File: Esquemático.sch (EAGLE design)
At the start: 4 parts, among them U1 MPU-6050-1, U2 MPU-6050-1, U3 MPU-6050-1

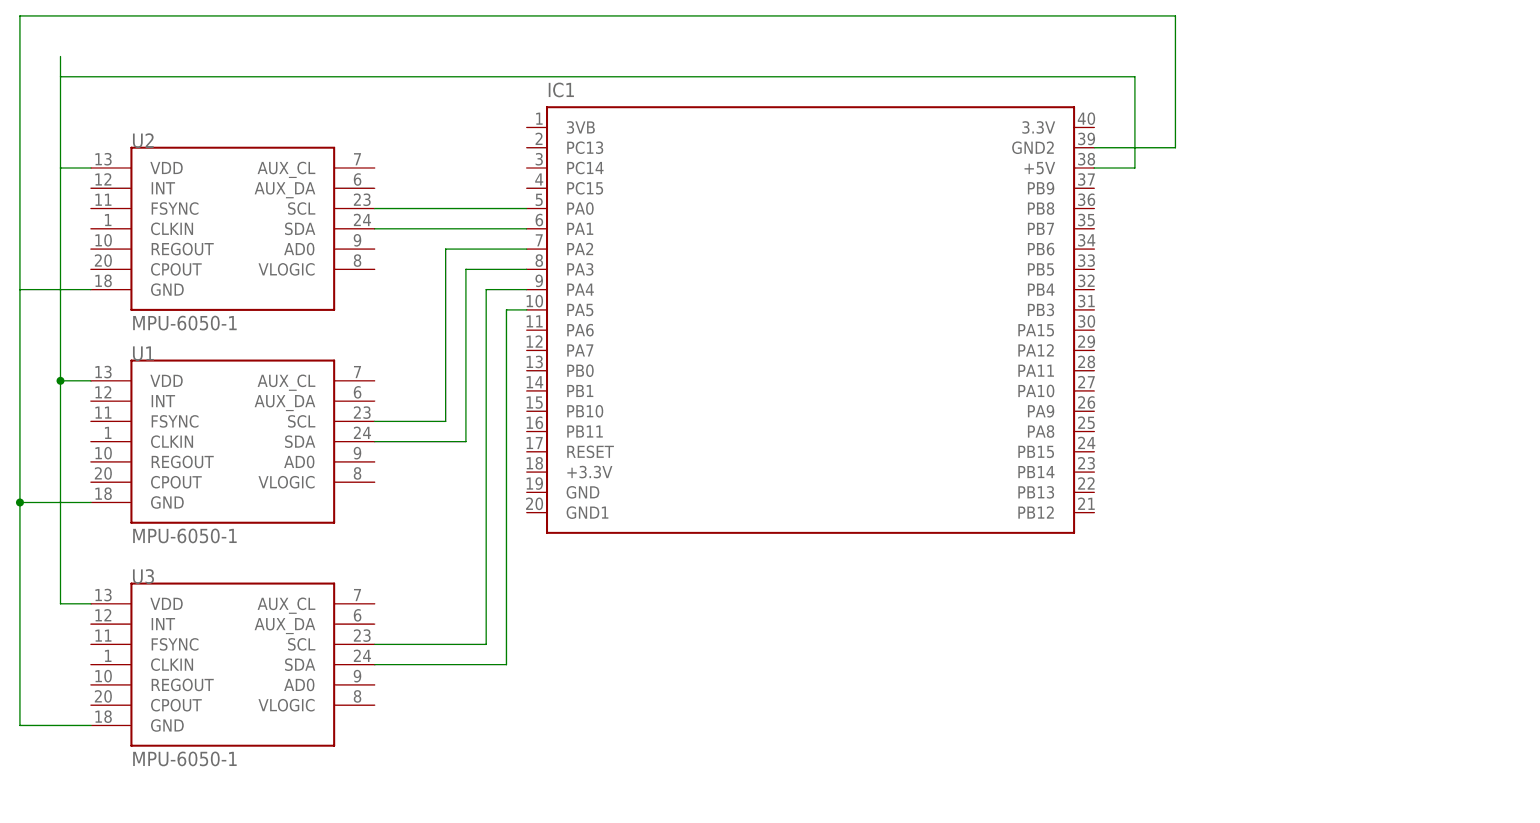
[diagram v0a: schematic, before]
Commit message: Esquemático
Agora usando comunicação I2C
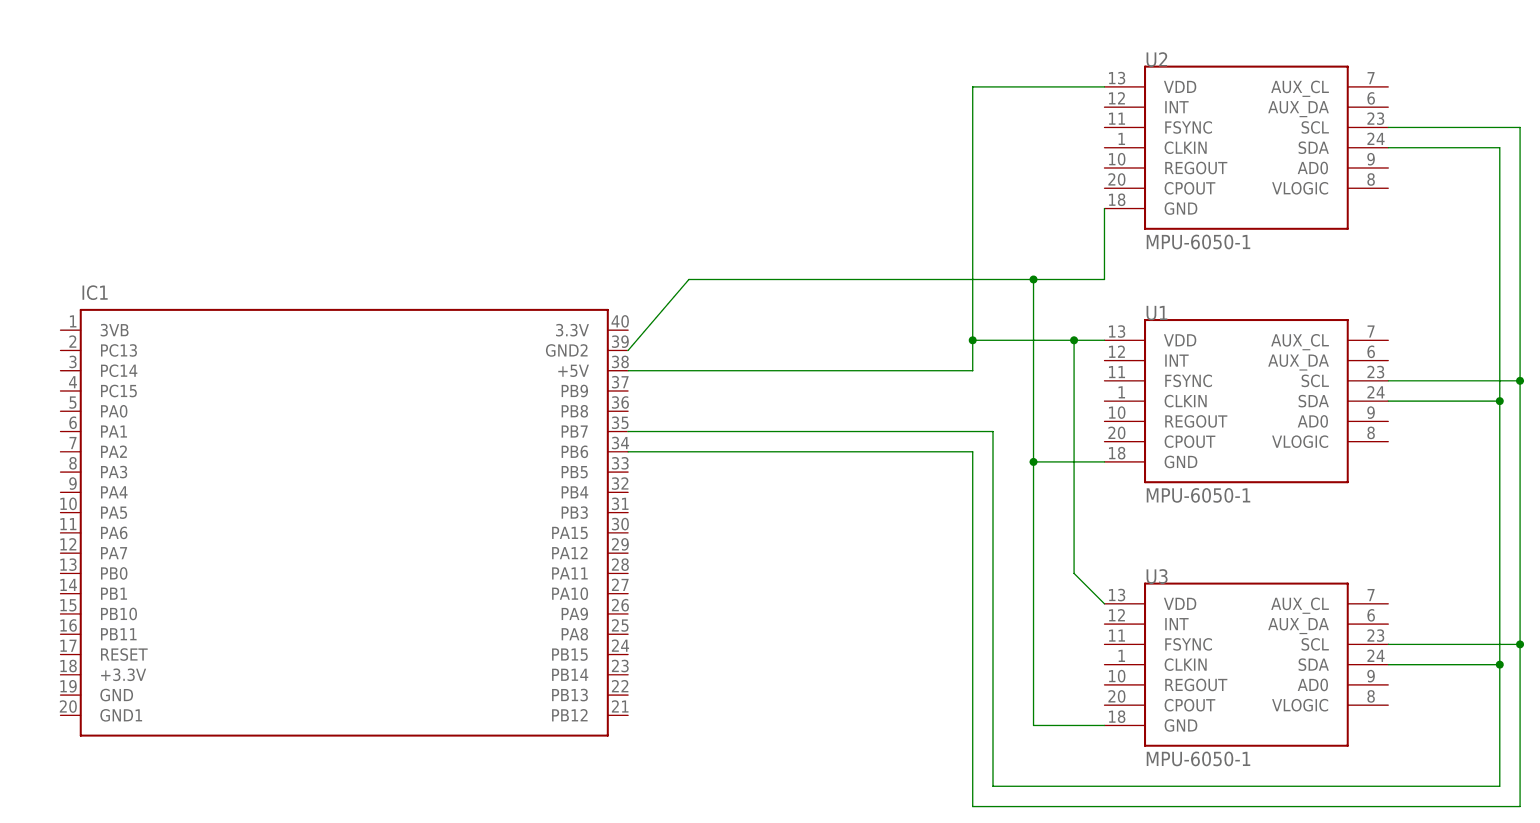
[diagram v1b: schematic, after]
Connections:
- removed net N$3 (its old number): IC1.PA2, U1.SCL
- removed net N$4 (its old number): IC1.PA3, U1.SDA
- removed net N$5: IC1.PA4, U3.SCL
- removed net N$6: IC1.PA5, U3.SDA
- net N$1: now also IC1.PB6, U1.SCL, U3.SCL; no longer IC1.PA0
- net N$2: now also IC1.PB7, U1.SDA, U3.SDA; no longer IC1.PA1
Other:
- moved on the sheet: IC1, U1, U2, U3
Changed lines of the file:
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@@
 <setting verticaltext="up"/>
 </settings>
-<grid distance="0.1" unitdist="inch" unit="inch" style="lines" multiple="1" display="yes" altdistance="0.01" altunitdist="inch" altunit="inch"/>
+<grid distance="0.1" unitdist="inch" unit="mm" style="lines" multiple="1" display="yes" altdistance="0.01" altunitdist="inch" altunit="inch"/>
 <layers>
 <layer number="1" name="Top" color="4" fill="1" visible="no" active="no"/>
@@
 </plain>
 <instances>
-<instance part="IC1" gate="G$1" x="30.48" y="52.07"/>
-<instance part="U1" gate="G$1" x="-41.91" y="38.1"/>
-<instance part="U2" gate="G$1" x="-41.91" y="64.77"/>
-<instance part="U3" gate="G$1" x="-41.91" y="10.16"/>
+<instance part="IC1" gate="G$1" x="-27.94" y="26.67"/>
+<instance part="U1" gate="G$1" x="85.09" y="43.18"/>
+<instance part="U2" gate="G$1" x="85.09" y="74.93"/>
+<instance part="U3" gate="G$1" x="85.09" y="10.16"/>
 </instances>
 <busses>
@@
 <net name="N$1" class="0">
 <segment>
+<pinref part="IC1" gate="G$1" pin="PB6"/>
+<wire x1="7.62" y1="36.83" x2="50.8" y2="36.83" width="0.1524" layer="91"/>
+<wire x1="50.8" y1="36.83" x2="50.8" y2="-7.62" width="0.1524" layer="91"/>
+<wire x1="50.8" y1="-7.62" x2="119.38" y2="-7.62" width="0.1524" layer="91"/>
+<wire x1="119.38" y1="-7.62" x2="119.38" y2="12.7" width="0.1524" layer="91"/>
 <pinref part="U2" gate="G$1" pin="SCL"/>
-<pinref part="IC1" gate="G$1" pin="PA0"/>
-<wire x1="-24.13" y1="67.31" x2="-5.08" y2="67.31" width="0.1524" layer="91"/>
+<wire x1="119.38" y1="12.7" x2="119.38" y2="45.72" width="0.1524" layer="91"/>
+<wire x1="119.38" y1="45.72" x2="119.38" y2="77.47" width="0.1524" layer="91"/>
+<wire x1="119.38" y1="77.47" x2="102.87" y2="77.47" width="0.1524" layer="91"/>
+<pinref part="U1" gate="G$1" pin="SCL"/>
+<wire x1="102.87" y1="45.72" x2="119.38" y2="45.72" width="0.1524" layer="91"/>
+<junction x="119.38" y="45.72"/>
+<pinref part="U3" gate="G$1" pin="SCL"/>
+<wire x1="102.87" y1="12.7" x2="119.38" y2="12.7" width="0.1524" layer="91"/>
+<junction x="119.38" y="12.7"/>
 </segment>
 </net>
 <net name="N$2" class="0">
 <segment>
+<pinref part="IC1" gate="G$1" pin="PB7"/>
+<wire x1="7.62" y1="39.37" x2="53.34" y2="39.37" width="0.1524" layer="91"/>
+<wire x1="53.34" y1="39.37" x2="53.34" y2="-5.08" width="0.1524" layer="91"/>
+<wire x1="53.34" y1="-5.08" x2="116.84" y2="-5.08" width="0.1524" layer="91"/>
 <pinref part="U2" gate="G$1" pin="SDA"/>
-<pinref part="IC1" gate="G$1" pin="PA1"/>
-<wire x1="-24.13" y1="64.77" x2="-5.08" y2="64.77" width="0.1524" layer="91"/>
+<wire x1="116.84" y1="-5.08" x2="116.84" y2="10.16" width="0.1524" layer="91"/>
+<wire x1="116.84" y1="10.16" x2="116.84" y2="43.18" width="0.1524" layer="91"/>
+<wire x1="116.84" y1="43.18" x2="116.84" y2="74.93" width="0.1524" layer="91"/>
+<wire x1="116.84" y1="74.93" x2="102.87" y2="74.93" width="0.1524" layer="91"/>
+<pinref part="U1" gate="G$1" pin="SDA"/>
+<wire x1="102.87" y1="43.18" x2="116.84" y2="43.18" width="0.1524" layer="91"/>
+<junction x="116.84" y="43.18"/>
+<pinref part="U3" gate="G$1" pin="SDA"/>
+<wire x1="102.87" y1="10.16" x2="116.84" y2="10.16" width="0.1524" layer="91"/>
+<junction x="116.84" y="10.16"/>
 </segment>
 </net>
 <net name="N$3" class="0">
 <segment>
-<pinref part="IC1" gate="G$1" pin="PA2"/>
-<wire x1="-5.08" y1="62.23" x2="-15.24" y2="62.23" width="0.1524" layer="91"/>
-<wire x1="-15.24" y1="62.23" x2="-15.24" y2="40.64" width="0.1524" layer="91"/>
-<pinref part="U1" gate="G$1" pin="SCL"/>
-<wire x1="-15.24" y1="40.64" x2="-24.13" y2="40.64" width="0.1524" layer="91"/>
+<pinref part="U2" gate="G$1" pin="VDD"/>
+<wire x1="67.31" y1="82.55" x2="50.8" y2="82.55" width="0.1524" layer="91"/>
+<wire x1="50.8" y1="82.55" x2="50.8" y2="50.8" width="0.1524" layer="91"/>
+<pinref part="IC1" gate="G$1" pin="+5V"/>
+<wire x1="50.8" y1="50.8" x2="50.8" y2="46.99" width="0.1524" layer="91"/>
+<wire x1="7.62" y1="46.99" x2="50.8" y2="46.99" width="0.1524" layer="91"/>
+<pinref part="U1" gate="G$1" pin="VDD"/>
+<wire x1="67.31" y1="50.8" x2="63.5" y2="50.8" width="0.1524" layer="91"/>
+<junction x="50.8" y="50.8"/>
+<pinref part="U3" gate="G$1" pin="VDD"/>
+<wire x1="63.5" y1="50.8" x2="50.8" y2="50.8" width="0.1524" layer="91"/>
+<wire x1="67.31" y1="17.78" x2="63.5" y2="21.59" width="0.1524" layer="91"/>
+<wire x1="63.5" y1="21.59" x2="63.5" y2="50.8" width="0.1524" layer="91"/>
+<junction x="63.5" y="50.8"/>
 </segment>
 </net>
 <net name="N$4" class="0">
 <segment>
-<pinref part="U1" gate="G$1" pin="SDA"/>
-<wire x1="-24.13" y1="38.1" x2="-12.7" y2="38.1" width="0.1524" layer="91"/>
-<wire x1="-12.7" y1="38.1" x2="-12.7" y2="59.69" width="0.1524" layer="91"/>
-<pinref part="IC1" gate="G$1" pin="PA3"/>
-<wire x1="-5.08" y1="59.69" x2="-12.7" y2="59.69" width="0.1524" layer="91"/>
-</segment>
-</net>
-<net name="N$5" class="0">
-<segment>
-<pinref part="IC1" gate="G$1" pin="PA4"/>
-<wire x1="-5.08" y1="57.15" x2="-10.16" y2="57.15" width="0.1524" layer="91"/>
-<pinref part="U3" gate="G$1" pin="SCL"/>
-<wire x1="-10.16" y1="57.15" x2="-10.16" y2="12.7" width="0.1524" layer="91"/>
-<wire x1="-10.16" y1="12.7" x2="-24.13" y2="12.7" width="0.1524" layer="91"/>
-</segment>
-</net>
-<net name="N$6" class="0">
-<segment>
-<pinref part="IC1" gate="G$1" pin="PA5"/>
-<wire x1="-5.08" y1="54.61" x2="-7.62" y2="54.61" width="0.1524" layer="91"/>
-<wire x1="-7.62" y1="54.61" x2="-7.62" y2="10.16" width="0.1524" layer="91"/>
-<pinref part="U3" gate="G$1" pin="SDA"/>
-<wire x1="-7.62" y1="10.16" x2="-24.13" y2="10.16" width="0.1524" layer="91"/>
-</segment>
-</net>
-<net name="N$7" class="0">
-<segment>
-<pinref part="U2" gate="G$1" pin="VDD"/>
-<wire x1="-59.69" y1="72.39" x2="-63.5" y2="72.39" width="0.1524" layer="91"/>
-<wire x1="-63.5" y1="72.39" x2="-63.5" y2="83.82" width="0.1524" layer="91"/>
-<wire x1="-63.5" y1="86.36" x2="-63.5" y2="83.82" width="0.1524" layer="91"/>
-<wire x1="-63.5" y1="83.82" x2="71.12" y2="83.82" width="0.1524" layer="91"/>
-<pinref part="IC1" gate="G$1" pin="+5V"/>
-<wire x1="71.12" y1="83.82" x2="71.12" y2="72.39" width="0.1524" layer="91"/>
-<wire x1="71.12" y1="72.39" x2="66.04" y2="72.39" width="0.1524" layer="91"/>
-<pinref part="U1" gate="G$1" pin="VDD"/>
-<wire x1="-59.69" y1="45.72" x2="-63.5" y2="45.72" width="0.1524" layer="91"/>
-<wire x1="-63.5" y1="45.72" x2="-63.5" y2="72.39" width="0.1524" layer="91"/>
-<pinref part="U3" gate="G$1" pin="VDD"/>
-<wire x1="-59.69" y1="17.78" x2="-63.5" y2="17.78" width="0.1524" layer="91"/>
-<wire x1="-63.5" y1="17.78" x2="-63.5" y2="45.72" width="0.1524" layer="91"/>
-<junction x="-63.5" y="45.72"/>
-</segment>
-</net>
-<net name="N$8" class="0">
-<segment>
+<pinref part="U1" gate="G$1" pin="GND"/>
+<wire x1="67.31" y1="35.56" x2="58.42" y2="35.56" width="0.1524" layer="91"/>
+<wire x1="58.42" y1="35.56" x2="58.42" y2="58.42" width="0.1524" layer="91"/>
+<wire x1="58.42" y1="58.42" x2="15.24" y2="58.42" width="0.1524" layer="91"/>
 <pinref part="IC1" gate="G$1" pin="GND2"/>
-<wire x1="66.04" y1="74.93" x2="76.2" y2="74.93" width="0.1524" layer="91"/>
-<wire x1="76.2" y1="74.93" x2="76.2" y2="91.44" width="0.1524" layer="91"/>
-<wire x1="76.2" y1="91.44" x2="-68.58" y2="91.44" width="0.1524" layer="91"/>
+<wire x1="15.24" y1="58.42" x2="7.62" y2="49.53" width="0.1524" layer="91"/>
 <pinref part="U2" gate="G$1" pin="GND"/>
-<wire x1="-68.58" y1="91.44" x2="-68.58" y2="57.15" width="0.1524" layer="91"/>
-<wire x1="-68.58" y1="57.15" x2="-59.69" y2="57.15" width="0.1524" layer="91"/>
-<pinref part="U1" gate="G$1" pin="GND"/>
-<wire x1="-59.69" y1="30.48" x2="-68.58" y2="30.48" width="0.1524" layer="91"/>
-<wire x1="-68.58" y1="30.48" x2="-68.58" y2="57.15" width="0.1524" layer="91"/>
+<wire x1="58.42" y1="58.42" x2="67.31" y2="58.42" width="0.1524" layer="91"/>
+<wire x1="67.31" y1="58.42" x2="67.31" y2="67.31" width="0.1524" layer="91"/>
+<junction x="58.42" y="58.42"/>
+<wire x1="58.42" y1="35.56" x2="58.42" y2="2.54" width="0.1524" layer="91"/>
+<junction x="58.42" y="35.56"/>
 <pinref part="U3" gate="G$1" pin="GND"/>
-<wire x1="-59.69" y1="2.54" x2="-68.58" y2="2.54" width="0.1524" layer="91"/>
-<wire x1="-68.58" y1="2.54" x2="-68.58" y2="30.48" width="0.1524" layer="91"/>
-<junction x="-68.58" y="30.48"/>
-</segment>
-</net>
+<wire x1="58.42" y1="2.54" x2="67.31" y2="2.54" width="0.1524" layer="91"/>
+</segment>
+</net>

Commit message: Última versão do Esquemático
Presentes tanto:
Esquemático.pdf
Esquemático.png
Esquemático.sch
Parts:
- removed U3: MPU-6050-1, Testing:MPU-6050-1
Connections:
- new net N$5: IC1.+5V, U1.VDD, U2.VDD
- new net N$6: IC1.GND2, U1.GND
- new net N$7: IC1.GND, U2.GND
- net N$1: now also IC1.PB10; no longer IC1.PB6, U1.SCL, U3.SCL
- net N$2: no longer U2.SDA, U3.SDA
- net N$3: now also IC1.PB6, U1.SCL; no longer IC1.+5V, U1.VDD, U2.VDD, U3.VDD
- net N$4: now also IC1.PB11, U2.SDA; no longer IC1.GND2, U1.GND, U2.GND, U3.GND
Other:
- moved on the sheet: IC1, U1, U2
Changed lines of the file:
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@@
 <part name="U1" library="Testing" deviceset="MPU-6050" device="-1"/>
 <part name="U2" library="Testing" deviceset="MPU-6050" device="-1"/>
-<part name="U3" library="Testing" deviceset="MPU-6050" device="-1"/>
 </parts>
 <sheets>
@@
 </plain>
 <instances>
-<instance part="IC1" gate="G$1" x="-27.94" y="26.67"/>
-<instance part="U1" gate="G$1" x="85.09" y="43.18"/>
-<instance part="U2" gate="G$1" x="85.09" y="74.93"/>
-<instance part="U3" gate="G$1" x="85.09" y="10.16"/>
+<instance part="IC1" gate="G$1" x="27.94" y="26.67"/>
+<instance part="U1" gate="G$1" x="90.17" y="71.12"/>
+<instance part="U2" gate="G$1" x="-46.99" y="13.97"/>
 </instances>
 <busses>
@@
 <net name="N$1" class="0">
 <segment>
+<pinref part="U2" gate="G$1" pin="SCL"/>
+<pinref part="IC1" gate="G$1" pin="PB10"/>
+<wire x1="-29.21" y1="16.51" x2="-7.62" y2="16.51" width="0.1524" layer="91"/>
+</segment>
+</net>
+<net name="N$3" class="0">
+<segment>
+<pinref part="U1" gate="G$1" pin="SCL"/>
+<wire x1="107.95" y1="73.66" x2="116.84" y2="73.66" width="0.1524" layer="91"/>
 <pinref part="IC1" gate="G$1" pin="PB6"/>
-<wire x1="7.62" y1="36.83" x2="50.8" y2="36.83" width="0.1524" layer="91"/>
-<wire x1="50.8" y1="36.83" x2="50.8" y2="-7.62" width="0.1524" layer="91"/>
-<wire x1="50.8" y1="-7.62" x2="119.38" y2="-7.62" width="0.1524" layer="91"/>
-<wire x1="119.38" y1="-7.62" x2="119.38" y2="12.7" width="0.1524" layer="91"/>
-<pinref part="U2" gate="G$1" pin="SCL"/>
-<wire x1="119.38" y1="12.7" x2="119.38" y2="45.72" width="0.1524" layer="91"/>
-<wire x1="119.38" y1="45.72" x2="119.38" y2="77.47" width="0.1524" layer="91"/>
-<wire x1="119.38" y1="77.47" x2="102.87" y2="77.47" width="0.1524" layer="91"/>
-<pinref part="U1" gate="G$1" pin="SCL"/>
-<wire x1="102.87" y1="45.72" x2="119.38" y2="45.72" width="0.1524" layer="91"/>
-<junction x="119.38" y="45.72"/>
-<pinref part="U3" gate="G$1" pin="SCL"/>
-<wire x1="102.87" y1="12.7" x2="119.38" y2="12.7" width="0.1524" layer="91"/>
-<junction x="119.38" y="12.7"/>
+<wire x1="63.5" y1="36.83" x2="116.84" y2="36.83" width="0.1524" layer="91"/>
+<wire x1="116.84" y1="36.83" x2="116.84" y2="73.66" width="0.1524" layer="91"/>
 </segment>
 </net>
@@
 <segment>
 <pinref part="IC1" gate="G$1" pin="PB7"/>
-<wire x1="7.62" y1="39.37" x2="53.34" y2="39.37" width="0.1524" layer="91"/>
-<wire x1="53.34" y1="39.37" x2="53.34" y2="-5.08" width="0.1524" layer="91"/>
-<wire x1="53.34" y1="-5.08" x2="116.84" y2="-5.08" width="0.1524" layer="91"/>
-<pinref part="U2" gate="G$1" pin="SDA"/>
-<wire x1="116.84" y1="-5.08" x2="116.84" y2="10.16" width="0.1524" layer="91"/>
-<wire x1="116.84" y1="10.16" x2="116.84" y2="43.18" width="0.1524" layer="91"/>
-<wire x1="116.84" y1="43.18" x2="116.84" y2="74.93" width="0.1524" layer="91"/>
-<wire x1="116.84" y1="74.93" x2="102.87" y2="74.93" width="0.1524" layer="91"/>
+<wire x1="63.5" y1="39.37" x2="114.3" y2="39.37" width="0.1524" layer="91"/>
+<wire x1="114.3" y1="39.37" x2="114.3" y2="71.12" width="0.1524" layer="91"/>
 <pinref part="U1" gate="G$1" pin="SDA"/>
-<wire x1="102.87" y1="43.18" x2="116.84" y2="43.18" width="0.1524" layer="91"/>
-<junction x="116.84" y="43.18"/>
-<pinref part="U3" gate="G$1" pin="SDA"/>
-<wire x1="102.87" y1="10.16" x2="116.84" y2="10.16" width="0.1524" layer="91"/>
-<junction x="116.84" y="10.16"/>
-</segment>
-</net>
-<net name="N$3" class="0">
-<segment>
-<pinref part="U2" gate="G$1" pin="VDD"/>
-<wire x1="67.31" y1="82.55" x2="50.8" y2="82.55" width="0.1524" layer="91"/>
-<wire x1="50.8" y1="82.55" x2="50.8" y2="50.8" width="0.1524" layer="91"/>
-<pinref part="IC1" gate="G$1" pin="+5V"/>
-<wire x1="50.8" y1="50.8" x2="50.8" y2="46.99" width="0.1524" layer="91"/>
-<wire x1="7.62" y1="46.99" x2="50.8" y2="46.99" width="0.1524" layer="91"/>
-<pinref part="U1" gate="G$1" pin="VDD"/>
-<wire x1="67.31" y1="50.8" x2="63.5" y2="50.8" width="0.1524" layer="91"/>
-<junction x="50.8" y="50.8"/>
-<pinref part="U3" gate="G$1" pin="VDD"/>
-<wire x1="63.5" y1="50.8" x2="50.8" y2="50.8" width="0.1524" layer="91"/>
-<wire x1="67.31" y1="17.78" x2="63.5" y2="21.59" width="0.1524" layer="91"/>
-<wire x1="63.5" y1="21.59" x2="63.5" y2="50.8" width="0.1524" layer="91"/>
-<junction x="63.5" y="50.8"/>
+<wire x1="114.3" y1="71.12" x2="107.95" y2="71.12" width="0.1524" layer="91"/>
 </segment>
 </net>
 <net name="N$4" class="0">
 <segment>
-<pinref part="U1" gate="G$1" pin="GND"/>
-<wire x1="67.31" y1="35.56" x2="58.42" y2="35.56" width="0.1524" layer="91"/>
-<wire x1="58.42" y1="35.56" x2="58.42" y2="58.42" width="0.1524" layer="91"/>
-<wire x1="58.42" y1="58.42" x2="15.24" y2="58.42" width="0.1524" layer="91"/>
-<pinref part="IC1" gate="G$1" pin="GND2"/>
-<wire x1="15.24" y1="58.42" x2="7.62" y2="49.53" width="0.1524" layer="91"/>
-<pinref part="U2" gate="G$1" pin="GND"/>
-<wire x1="58.42" y1="58.42" x2="67.31" y2="58.42" width="0.1524" layer="91"/>
-<wire x1="67.31" y1="58.42" x2="67.31" y2="67.31" width="0.1524" layer="91"/>
-<junction x="58.42" y="58.42"/>
-<wire x1="58.42" y1="35.56" x2="58.42" y2="2.54" width="0.1524" layer="91"/>
-<junction x="58.42" y="35.56"/>
-<pinref part="U3" gate="G$1" pin="GND"/>
-<wire x1="58.42" y1="2.54" x2="67.31" y2="2.54" width="0.1524" layer="91"/>
+<pinref part="U2" gate="G$1" pin="SDA"/>
+<pinref part="IC1" gate="G$1" pin="PB11"/>
+<wire x1="-29.21" y1="13.97" x2="-7.62" y2="13.97" width="0.1524" layer="91"/>
 </segment>
 </net>
+<net name="N$5" class="0">
+<segment>
+<pinref part="U1" gate="G$1" pin="VDD"/>
+<wire x1="72.39" y1="78.74" x2="68.58" y2="78.74" width="0.1524" layer="91"/>
+<pinref part="IC1" gate="G$1" pin="+5V"/>
+<wire x1="63.5" y1="46.99" x2="68.58" y2="46.99" width="0.1524" layer="91"/>
+<wire x1="68.58" y1="46.99" x2="68.58" y2="60.96" width="0.1524" layer="91"/>
+<pinref part="U2" gate="G$1" pin="VDD"/>
+<wire x1="68.58" y1="60.96" x2="68.58" y2="78.74" width="0.1524" layer="91"/>
+<wire x1="68.58" y1="60.96" x2="-64.77" y2="60.96" width="0.1524" layer="91"/>
+<wire x1="-64.77" y1="60.96" x2="-64.77" y2="21.59" width="0.1524" layer="91"/>
+<junction x="68.58" y="60.96"/>
+</segment>
+</net>
+<net name="N$6" class="0">
+<segment>
+<pinref part="U1" gate="G$1" pin="GND"/>
+<pinref part="IC1" gate="G$1" pin="GND2"/>
+<wire x1="72.39" y1="63.5" x2="72.39" y2="49.53" width="0.1524" layer="91"/>
+<wire x1="72.39" y1="49.53" x2="63.5" y2="49.53" width="0.1524" layer="91"/>
+</segment>
+</net>
+<net name="N$7" class="0">
+<segment>
+<pinref part="IC1" gate="G$1" pin="GND"/>
+<wire x1="-7.62" y1="6.35" x2="-15.24" y2="6.35" width="0.1524" layer="91"/>
+<wire x1="-15.24" y1="6.35" x2="-15.24" y2="0" width="0.1524" layer="91"/>
+<wire x1="-15.24" y1="0" x2="-66.04" y2="0" width="0.1524" layer="91"/>
+<pinref part="U2" gate="G$1" pin="GND"/>
+<wire x1="-66.04" y1="0" x2="-66.04" y2="6.35" width="0.1524" layer="91"/>
+<wire x1="-66.04" y1="6.35" x2="-64.77" y2="6.35" width="0.1524" layer="91"/>
+</segment>
+</net>
